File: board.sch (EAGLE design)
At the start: 2 parts

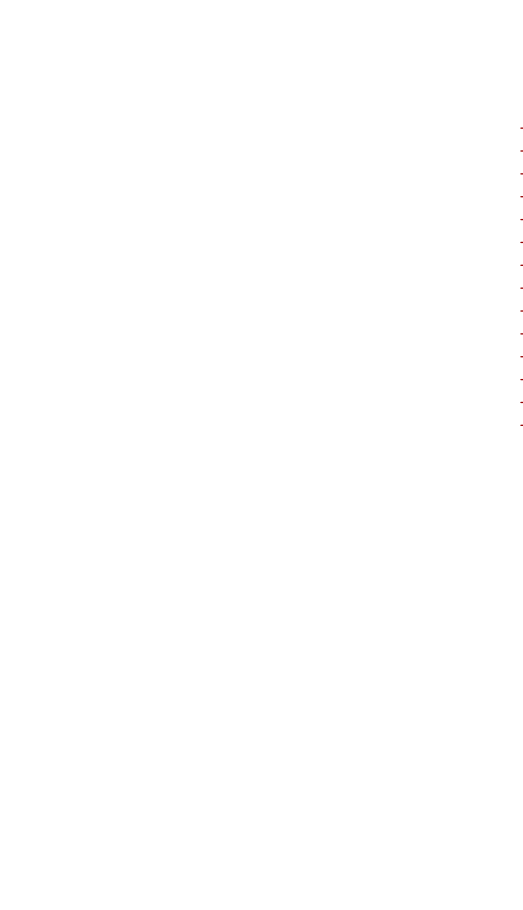
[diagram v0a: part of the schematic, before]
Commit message: added voltage divider circuit
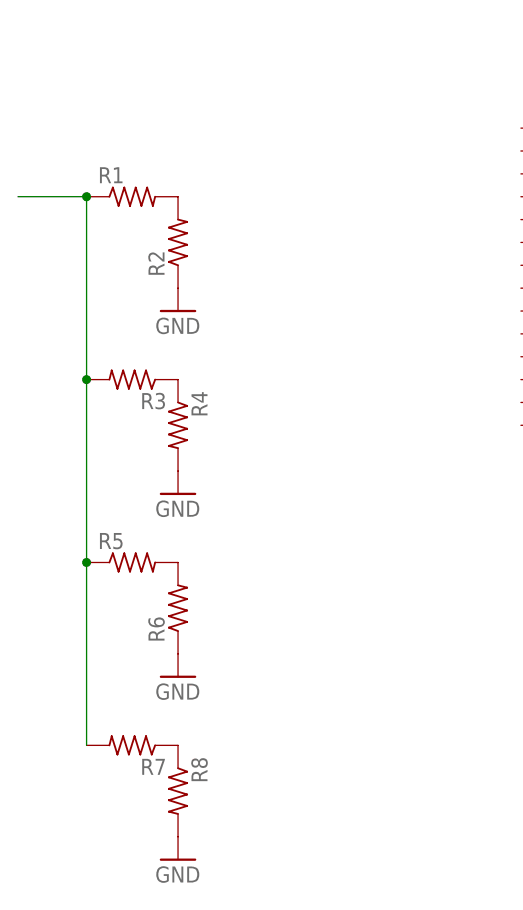
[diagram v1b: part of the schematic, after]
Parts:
- added R1, R2, R3, R4, R5, R6, R7, R8: (no value), rcl:R-US_0204/2V
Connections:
- new net GND: R2.1, R4.2, R6.1, R8.2
- new net N$1: R1.2, R2.2
- new net N$2: R3.1, R4.1
- new net N$3: R5.2, R6.2
- new net N$4: R7.1, R8.1
- new net N$5: R1.1, R3.2, R5.1, R7.2
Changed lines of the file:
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@@
 <part name="U$1" library="PIC24HJ128GP502DIP" deviceset="PIC24HJ128GP502_" device=""/>
 <part name="U$2" library="SparkFun" deviceset="SD_CARD_SOCKET" device="SD"/>
+<part name="R1" library="rcl" deviceset="R-US_" device="0204/2V"/>
+<part name="R2" library="rcl" deviceset="R-US_" device="0204/2V"/>
+<part name="R3" library="rcl" deviceset="R-US_" device="0204/2V"/>
+<part name="R4" library="rcl" deviceset="R-US_" device="0204/2V"/>
+<part name="R5" library="rcl" deviceset="R-US_" device="0204/2V"/>
+<part name="R6" library="rcl" deviceset="R-US_" device="0204/2V"/>
+<part name="R7" library="rcl" deviceset="R-US_" device="0204/2V"/>
+<part name="R8" library="rcl" deviceset="R-US_" device="0204/2V"/>
+<part name="GND1" library="supply1" deviceset="GND" device=""/>
+<part name="GND2" library="supply1" deviceset="GND" device=""/>
+<part name="GND3" library="supply1" deviceset="GND" device=""/>
+<part name="GND4" library="supply1" deviceset="GND" device=""/>
 </parts>
 <sheets>
@@
 <instance part="U$1" gate="A" x="-7.62" y="60.96"/>
 <instance part="U$2" gate="G$1" x="233.68" y="48.26"/>
+<instance part="R1" gate="G$1" x="-50.8" y="53.34"/>
+<instance part="R2" gate="G$1" x="-45.72" y="48.26" rot="R90"/>
+<instance part="R3" gate="G$1" x="-50.8" y="33.02" rot="R180"/>
+<instance part="R4" gate="G$1" x="-45.72" y="27.94" rot="R270"/>
+<instance part="R5" gate="G$1" x="-50.8" y="12.7"/>
+<instance part="R6" gate="G$1" x="-45.72" y="7.62" rot="R90"/>
+<instance part="R7" gate="G$1" x="-50.8" y="-7.62" rot="R180"/>
+<instance part="R8" gate="G$1" x="-45.72" y="-12.7" rot="R270"/>
+<instance part="GND1" gate="1" x="-45.72" y="40.64"/>
+<instance part="GND2" gate="1" x="-45.72" y="20.32"/>
+<instance part="GND3" gate="1" x="-45.72" y="0"/>
+<instance part="GND4" gate="1" x="-45.72" y="-20.32"/>
 </instances>
 <busses>
 </busses>
 <nets>
+<net name="N$1" class="0">
+<segment>
+<pinref part="R1" gate="G$1" pin="2"/>
+<pinref part="R2" gate="G$1" pin="2"/>
+</segment>
+</net>
+<net name="N$2" class="0">
+<segment>
+<pinref part="R3" gate="G$1" pin="1"/>
+<pinref part="R4" gate="G$1" pin="1"/>
+</segment>
+</net>
+<net name="N$3" class="0">
+<segment>
+<pinref part="R5" gate="G$1" pin="2"/>
+<pinref part="R6" gate="G$1" pin="2"/>
+</segment>
+</net>
+<net name="N$4" class="0">
+<segment>
+<pinref part="R7" gate="G$1" pin="1"/>
+<pinref part="R8" gate="G$1" pin="1"/>
+</segment>
+</net>
+<net name="GND" class="0">
+<segment>
+<pinref part="R2" gate="G$1" pin="1"/>
+<pinref part="GND1" gate="1" pin="GND"/>
+</segment>
+<segment>
+<pinref part="R4" gate="G$1" pin="2"/>
+<pinref part="GND2" gate="1" pin="GND"/>
+</segment>
+<segment>
+<pinref part="R6" gate="G$1" pin="1"/>
+<pinref part="GND3" gate="1" pin="GND"/>
+</segment>
+<segment>
+<pinref part="R8" gate="G$1" pin="2"/>
+<pinref part="GND4" gate="1" pin="GND"/>
+</segment>
+</net>
+<net name="N$5" class="0">
+<segment>
+<pinref part="R1" gate="G$1" pin="1"/>
+<pinref part="R3" gate="G$1" pin="2"/>
+<wire x1="-55.88" y1="53.34" x2="-55.88" y2="33.02" width="0.1524" layer="91"/>
+<pinref part="R5" gate="G$1" pin="1"/>
+<wire x1="-55.88" y1="12.7" x2="-55.88" y2="33.02" width="0.1524" layer="91"/>
+<junction x="-55.88" y="33.02"/>
+<pinref part="R7" gate="G$1" pin="2"/>
+<wire x1="-55.88" y1="-7.62" x2="-55.88" y2="12.7" width="0.1524" layer="91"/>
+<junction x="-55.88" y="12.7"/>
+<wire x1="-55.88" y1="53.34" x2="-63.5" y2="53.34" width="0.1524" layer="91"/>
+<junction x="-55.88" y="53.34"/>
+</segment>
+</net>
 </nets>
 </sheet>

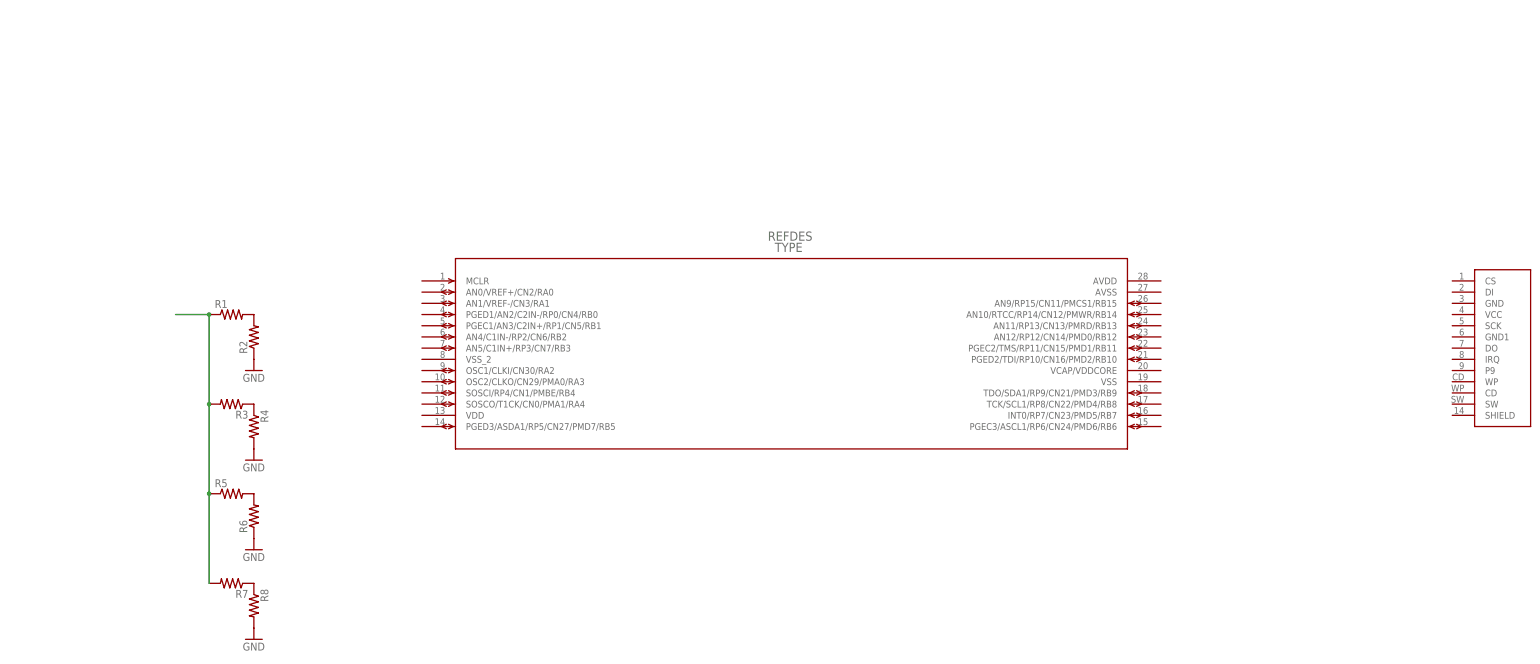
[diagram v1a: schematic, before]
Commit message: added the output stage and vco to the layout
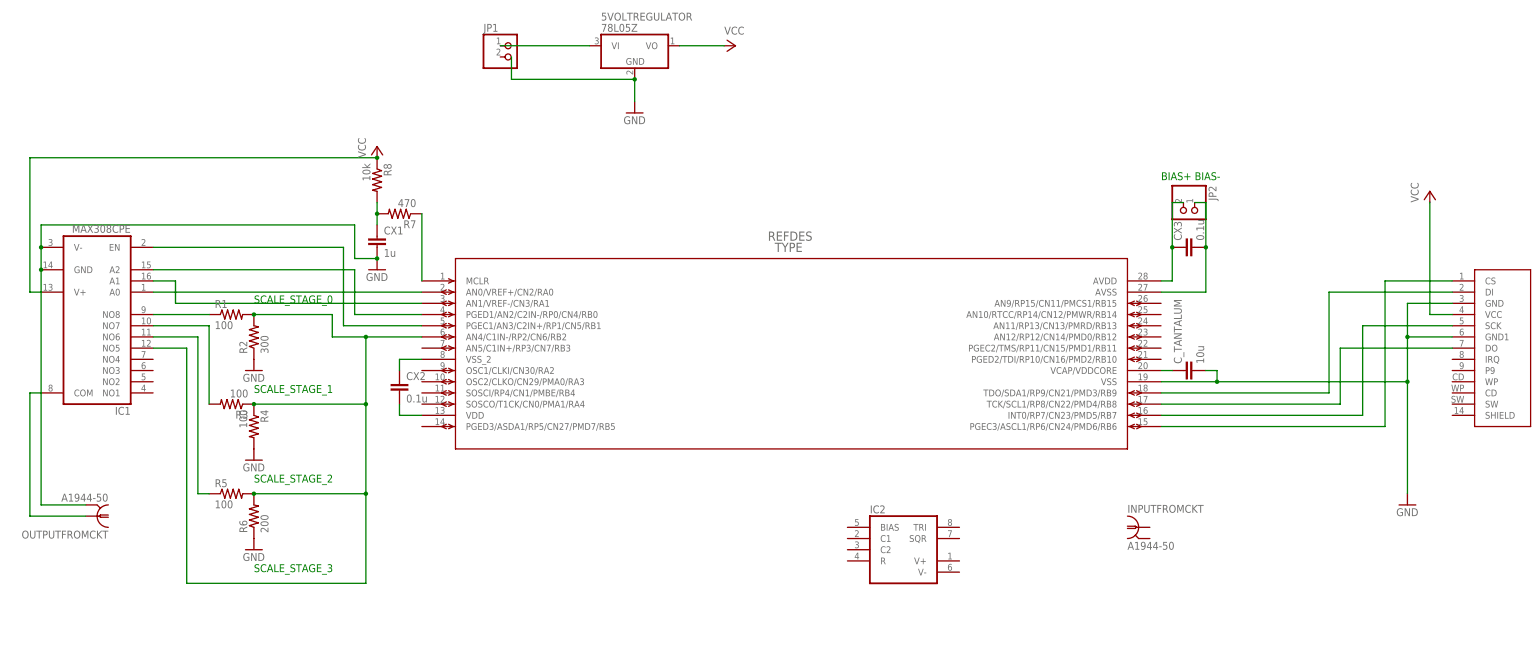
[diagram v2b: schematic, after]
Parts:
- added 5VOLTREGULATOR: 78L05Z, linear:78L05Z
- added CX1: 1u, resistor:CXXC10B5
- added CX2, CX3: 0.1u, resistor:CXXC10B5
- added C_TANTALUM: 10u, resistor:CXXC10B5
- added IC1: MAX308CPE, maxim:MAX308CPE
- added IC2: (no value), exar:XR-2209
- added INPUTFROMCKT, OUTPUTFROMCKT: A1944-50, con-coax:A1944-50
- added JP1, JP2: (no value), pinhead:PINHD-1X2/90
- R1, R3, R4, R5: value (none) -> 100
- R2: value (none) -> 300
- R6: value (none) -> 200
- R7: value (none) -> 470; device rcl:R-US_0204/2V -> resistor:R-US_0204/7
- R8: value (none) -> 10k; device rcl:R-US_0204/2V -> resistor:R-US_0204/7
- renumbered U$1 to PIC24HJ128GP502, U$2 to SDCARD
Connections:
- new net ADC: IC1.NO5, PIC24HJ128GP502.AN4/C1IN-/RP2/CN6/RB2, R1.2, R2.2, R3.1, R4.1, R5.2, R6.2
- new net AVDD: CX3.1, JP2.2, PIC24HJ128GP502.AVDD
- new net AVSS: CX3.2, JP2.1, PIC24HJ128GP502.AVSS
- new net N$10: CX2.2, PIC24HJ128GP502.VDD
- new net N$11: IC1.A0, PIC24HJ128GP502.AN0/VREF+/CN2/RA0
- new net N$12: IC1.A1, PIC24HJ128GP502.AN1/VREF-/CN3/RA1
- new net N$13: IC1.COM, OUTPUTFROMCKTG$1.1
- new net N$14: IC1.A2, PIC24HJ128GP502.PGED1/AN2/C2IN-/RP0/CN4/RB0
- new net N$15: IC1.NO7, R3.2
- new net N$16: IC1.NO6, R5.1
- new net N$17: IC1.EN, PIC24HJ128GP502.PGEC1/AN3/C2IN+/RP1/CN5/RB1
- new net N$18: 5VOLTREGULATOR.VI, JP1.1
- new net N$6: PIC24HJ128GP502.INT0/RP7/CN23/PMD5/RB7, SDCARD.SCK
- new net N$7: PIC24HJ128GP502.TDO/SDA1/RP9/CN21/PMD3/RB9, SDCARD.DI
- new net N$8: PIC24HJ128GP502.TCK/SCL1/RP8/CN22/PMD4/RB8, SDCARD.DO
- new net N$9: PIC24HJ128GP502.PGEC3/ASCL1/RP6/CN24/PMD6/RB6, SDCARD.CS
- new net VCC: 5VOLTREGULATOR.VO, IC1.V+, R8.1, SDCARD.VCC
- net GND: now also 5VOLTREGULATOR.GND, CX1.2, C_TANTALUM.2, IC1.GND, IC1.V-, OUTPUTFROMCKTG$1.GND, PIC24HJ128GP502.VSS, SDCARD.GND, SDCARD.GND1; no longer R8.2
- net N$1: now also IC1.NO8, R1.1; no longer R1.2, R2.2
- net N$2: now also PIC24HJ128GP502.MCLR, R7.1; no longer R3.1, R4.1
- net N$3: now also CX1.1, R7.2, R8.2; no longer R5.2, R6.2
- net N$4: now also C_TANTALUM.1, PIC24HJ128GP502.VCAP/VDDCORE; no longer R7.1, R8.1
- net N$5: now also CX2.1, PIC24HJ128GP502.VSS_2; no longer R1.1, R3.2, R5.1, R7.2
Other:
- note added: "BIAS+"
- note added: "BIAS-"
- note added: "SCALE_STAGE_0"
- note added: "SCALE_STAGE_1"
- note added: "SCALE_STAGE_2"
- note added: "SCALE_STAGE_3"
- moved on the sheet: R7, R8

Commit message: Added lcd and buttons
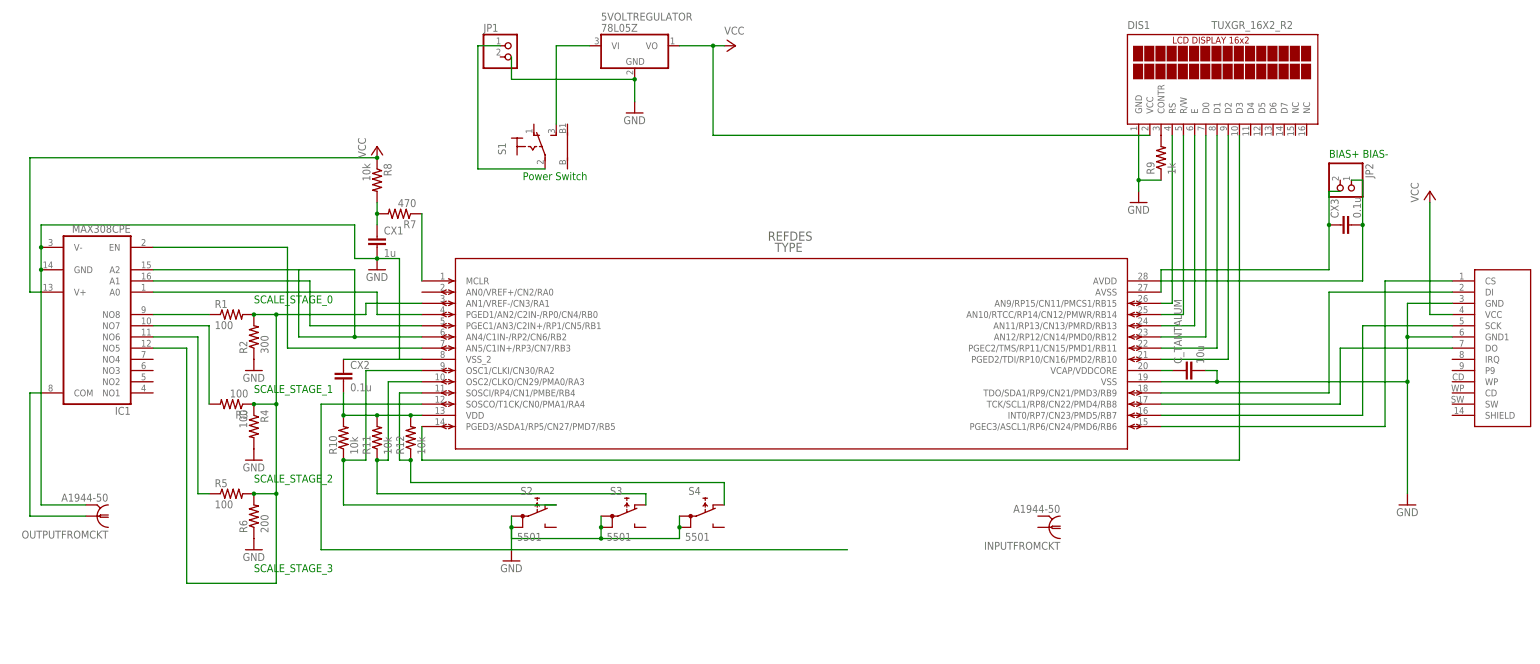
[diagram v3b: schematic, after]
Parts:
- removed IC2: (no value), exar:XR-2209
- added DIS1: TUXGR_16X2_R2, display-lcd:TUXGR_16X2_R2
- added R10, R11, R12: 10k, rcl:R-US_0204/2V
- added R9: 1k, resistor:R-US_0204/2V
- added S1: (no value), switch:316-917
- added S2, S3, S4: 5501, switch:5501
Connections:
- net AVSS renamed N$19
- removed net AVDD: CX3.1, JP2.2, PIC24HJ128GP502.AVDD
- removed net N$5: CX2.1, PIC24HJ128GP502.VSS_2
- new net DECREASE_BUTTON: PIC24HJ128GP502.SOSCI/RP4/CN1/PMBE/RB4, R12.1, S4.NC
- new net EXECUTE_BUTTON: PIC24HJ128GP502.OSC1/CLKI/CN30/RA2, R10.1, S2.NC
- new net INCREASE_BUTTON: PIC24HJ128GP502.OSC2/CLKO/CN29/PMA0/RA3, R11.1, S3.NC
- new net LCD_D0: DIS1.D0, PIC24HJ128GP502.AN12/RP12/CN14/PMD0/RB12
- new net LCD_D1: DIS1.D1, PIC24HJ128GP502.PGEC2/TMS/RP11/CN15/PMD1/RB11
- new net LCD_D2: DIS1.D2, PIC24HJ128GP502.PGED2/TDI/RP10/CN16/PMD2/RB10
- new net LCD_D3: DIS1.D3, PIC24HJ128GP502.PGED3/ASDA1/RP5/CN27/PMD7/RB5
- new net LCD_E: DIS1.E, PIC24HJ128GP502.AN11/RP13/CN13/PMRD/RB13
- new net LCD_RS: DIS1.RS, PIC24HJ128GP502.AN9/RP15/CN11/PMCS1/RB15
- new net LCD_RW: DIS1.R/W, PIC24HJ128GP502.AN10/RTCC/RP14/CN12/PMWR/RB14
- new net N$20: CX3.1, PIC24HJ128GP502.AVDD
- new net N$21: JP1.1, S1.P
- new net N$27: DIS1.CONTR, R9.2
- new net VCO: PIC24HJ128GP502.SOSCO/T1CK/CN0/PMA1/RA4
- net ADC: now also PIC24HJ128GP502.AN1/VREF-/CN3/RA1; no longer PIC24HJ128GP502.AN4/C1IN-/RP2/CN6/RB2
- net GND: now also CX2.1, DIS1.GND, PIC24HJ128GP502.VSS_2, R9.1, S2.1A, S2.1B, S3.1A, S3.1B, S4.1A, S4.1B
- net N$10: now also R10.2, R11.2, R12.2
- net N$11: now also IC1.EN, PIC24HJ128GP502.AN5/C1IN+/RP3/CN7/RB3; no longer IC1.A0, PIC24HJ128GP502.AN0/VREF+/CN2/RA0
- net N$12: now also IC1.A2, PIC24HJ128GP502.AN4/C1IN-/RP2/CN6/RB2; no longer IC1.A1, PIC24HJ128GP502.AN1/VREF-/CN3/RA1
- net N$14: now also IC1.A1, PIC24HJ128GP502.PGEC1/AN3/C2IN+/RP1/CN5/RB1; no longer IC1.A2, PIC24HJ128GP502.PGED1/AN2/C2IN-/RP0/CN4/RB0
- net N$17: now also IC1.A0, PIC24HJ128GP502.PGED1/AN2/C2IN-/RP0/CN4/RB0; no longer IC1.EN, PIC24HJ128GP502.PGEC1/AN3/C2IN+/RP1/CN5/RB1
- net N$18: now also S1.S; no longer JP1.1
- net VCC: now also DIS1.VCC
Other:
- note added: "Power Switch"
- moved on the sheet: CX2, CX3, INPUTFROMCKT, JP2

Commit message: Labeled all the components
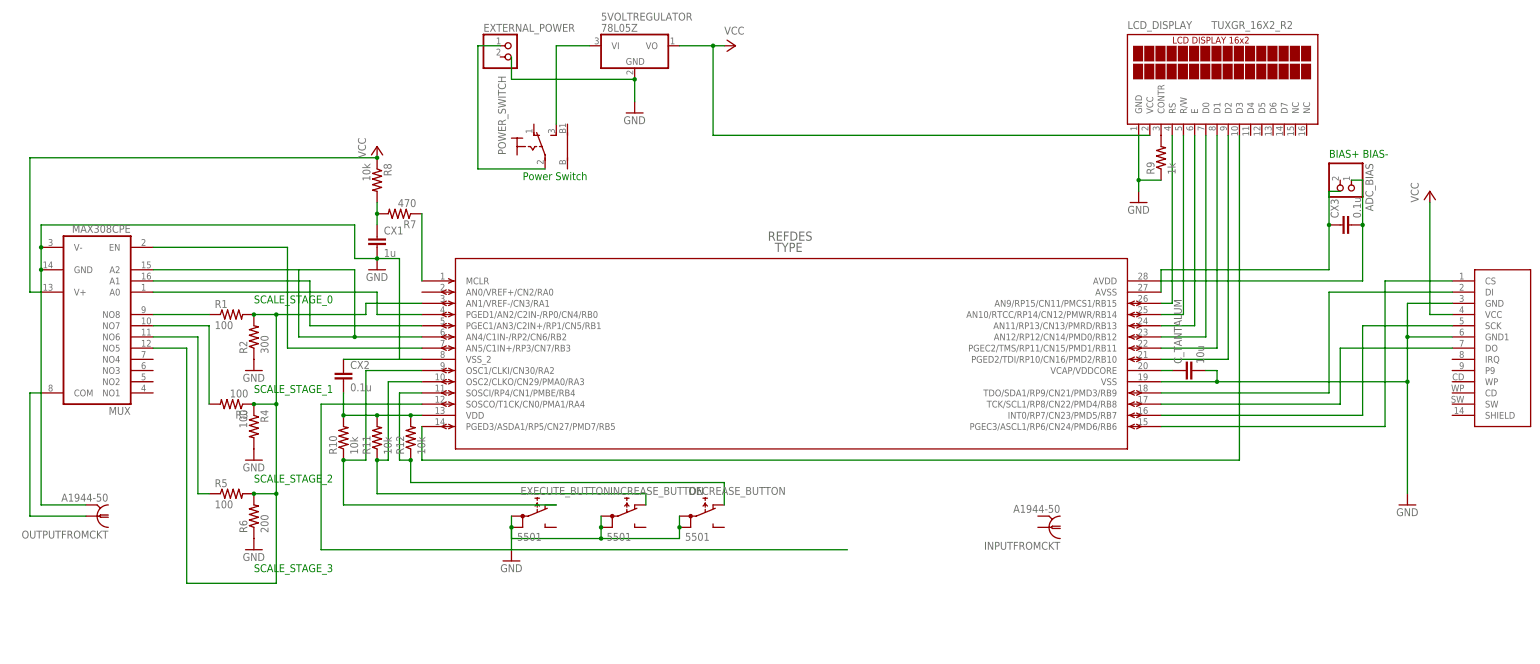
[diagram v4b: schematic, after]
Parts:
- renumbered DIS1 to LCD_DISPLAY, IC1 to MUX, JP1 to EXTERNAL_POWER, JP2 to ADC_BIAS, S1 to POWER_SWITCH, S2 to EXECUTE_BUTTON, S3 to INCREASE_BUTTON, S4 to DECREASE_BUTTON

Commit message: Labeled all the nets in order to allow for a sensible pin list export
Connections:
- net N$1 renamed SCALE_0
- net N$11 renamed MUX_EN
- net N$12 renamed MUX_2
- net N$13 renamed OUTPUT_CKT
- net N$14 renamed MUX_1
- net N$15 renamed SCALE_1
- net N$16 renamed SCALE_2
- net N$17 renamed MUX_0
- net N$19 renamed ADC_BIAS-
- net N$20 renamed ADC_BIAS+
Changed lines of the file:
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@@
 </segment>
 </net>
-<net name="N$1" class="0">
+<net name="SCALE_0" class="0">
 <segment>
 <pinref part="R1" gate="G$1" pin="1"/>
@@
 </segment>
 </net>
-<net name="N$13" class="0">
+<net name="OUTPUT_CKT" class="0">
 <segment>
 <pinref part="OUTPUTFROMCKT" gate="G$1" pin="1"/>
@@
 </segment>
 </net>
-<net name="N$15" class="0">
+<net name="SCALE_1" class="0">
 <segment>
 <pinref part="R3" gate="G$1" pin="2"/>
@@
 </segment>
 </net>
-<net name="N$16" class="0">
+<net name="SCALE_2" class="0">
 <segment>
 <pinref part="R5" gate="G$1" pin="1"/>
@@
 </segment>
 </net>
-<net name="N$20" class="0">
+<net name="ADC_BIAS+" class="0">
 <segment>
 <pinref part="CX3" gate="G$1" pin="1"/>
@@
 </segment>
 </net>
-<net name="N$19" class="0">
+<net name="ADC_BIAS-" class="0">
 <segment>
 <pinref part="ADC_BIAS" gate="G$1" pin="1"/>
@@
 </segment>
 </net>
-<net name="N$11" class="0">
+<net name="MUX_EN" class="0">
 <segment>
 <pinref part="PIC24HJ128GP502" gate="A" pin="AN5/C1IN+/RP3/CN7/RB3"/>
@@
 </segment>
 </net>
-<net name="N$12" class="0">
+<net name="MUX_2" class="0">
 <segment>
 <pinref part="PIC24HJ128GP502" gate="A" pin="AN4/C1IN-/RP2/CN6/RB2"/>
@@
 </segment>
 </net>
-<net name="N$14" class="0">
+<net name="MUX_1" class="0">
 <segment>
 <pinref part="PIC24HJ128GP502" gate="A" pin="PGEC1/AN3/C2IN+/RP1/CN5/RB1"/>
@@
 </segment>
 </net>
-<net name="N$17" class="0">
+<net name="MUX_0" class="0">
 <segment>
 <pinref part="PIC24HJ128GP502" gate="A" pin="PGED1/AN2/C2IN-/RP0/CN4/RB0"/>
